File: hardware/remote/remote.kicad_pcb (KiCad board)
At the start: 2 copper layers, 106.7 x 86.4 mm, 30 parts

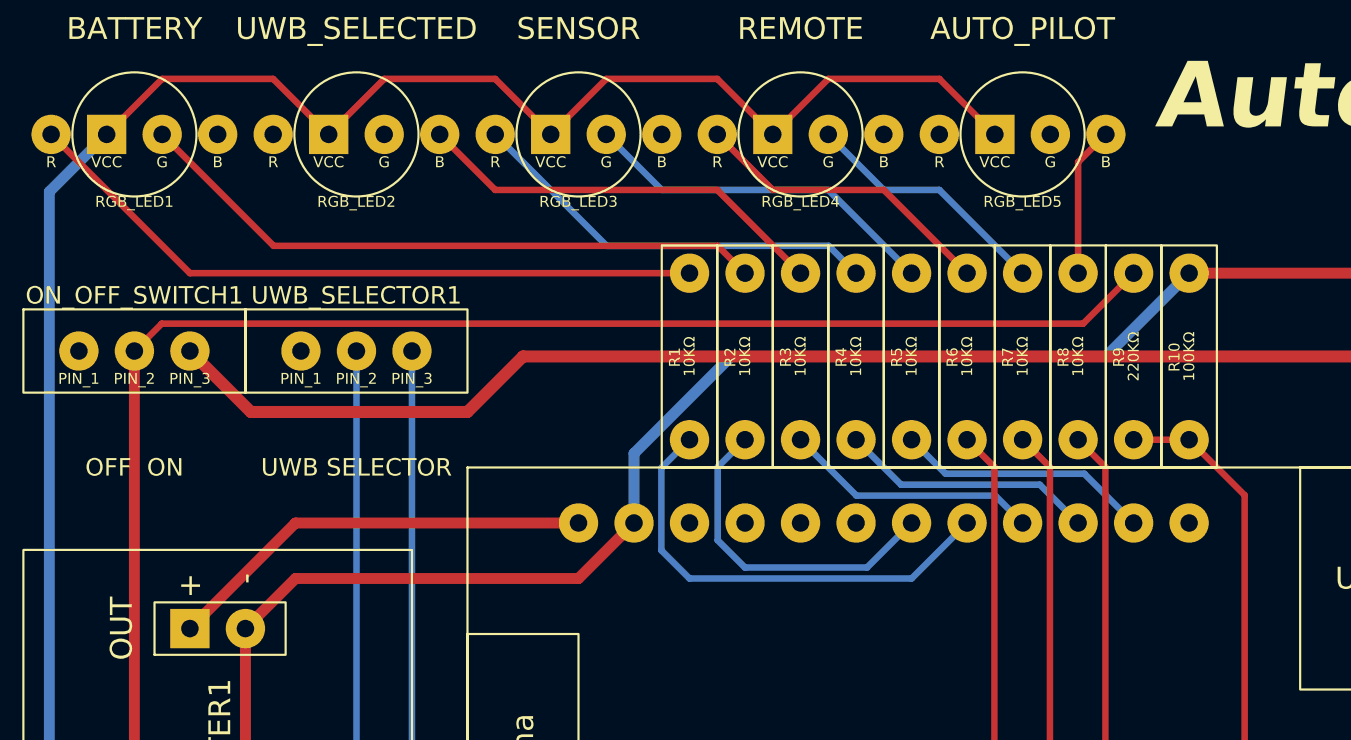
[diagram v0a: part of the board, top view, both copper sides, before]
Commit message: hardware: Update pcd design for better wiring clearance.
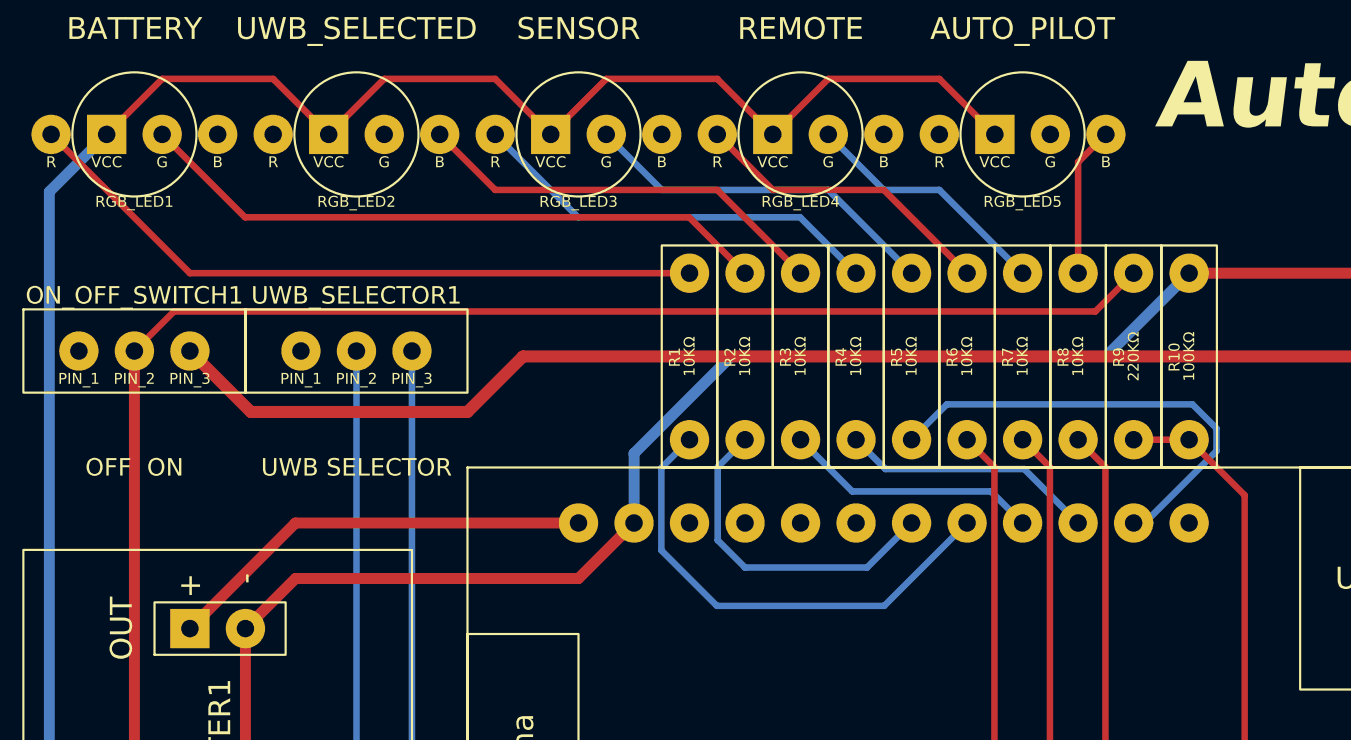
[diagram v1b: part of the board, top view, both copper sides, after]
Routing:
- net Net-(ESP32_UWB1-IO22): track 11.7 -> 22.0 mm
- net Net-(ESP32_UWB1-IO16): track 21.2 -> 22.2 mm
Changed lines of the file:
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@@
+	)
+	(segment
+		(start 70.657127 32.250873)
+		(end 72.409 30.499)
+		(width 0.3)
+		(layer "F.Cu")
+		(net 8)
 	)
 	(segment
 		(start 26.689 34.060058)
-		(end 27.94 32.809058)
+		(end 28.498185 32.250873)
 		(width 0.3)
 		(layer "F.Cu")
@@
 	)
 	(segment
-		(start 27.94 32.809058)
-		(end 70.098942 32.809058)
-		(width 0.3)
-		(layer "F.Cu")
-		(net 8)
-	)
-	(segment
-		(start 70.098942 32.809058)
-		(end 72.409 30.499)
+		(start 28.498185 32.250873)
+		(end 70.657127 32.250873)
 		(width 0.3)
 		(layer "F.Cu")
@@
 	)
 	(segment
-		(start 33.058 29.248)
-		(end 53.378 29.248)
+		(start 52.07 27.94)
+		(end 54.629 30.499)
 		(width 0.3)
 		(layer "F.Cu")
@@
 	)
 	(segment
+		(start 31.75 27.94)
+		(end 52.07 27.94)
+		(width 0.3)
+		(layer "F.Cu")
+		(net 37)
+	)
+	(segment
 		(start 27.959 24.149)
-		(end 33.058 29.248)
-		(width 0.3)
-		(layer "F.Cu")
-		(net 37)
-	)
-	(segment
-		(start 53.378 29.248)
-		(end 54.629 30.499)
+		(end 31.75 27.94)
 		(width 0.3)
 		(layer "F.Cu")
@@
 	)
 	(segment
-		(start 59.728 40.678)
-		(end 66.078 40.678)
+		(start 65.88331 40.48331)
+		(end 67.329 41.929)
 		(width 0.3)
 		(layer "B.Cu")
@@
 	)
 	(segment
+		(start 59.53331 40.48331)
+		(end 65.88331 40.48331)
+		(width 0.3)
+		(layer "B.Cu")
+		(net 44)
+	)
+	(segment
 		(start 57.169 38.119)
-		(end 59.728 40.678)
+		(end 59.53331 40.48331)
 		(width 0.3)
 		(layer "B.Cu")
@@
 	)
 	(segment
-		(start 66.078 40.678)
-		(end 67.329 41.929)
-		(width 0.3)
-		(layer "B.Cu")
-		(net 44)
+		(start 61.049231 39.459231)
+		(end 67.399231 39.459231)
+		(width 0.3)
+		(layer "B.Cu")
+		(net 45)
+	)
+	(segment
+		(start 67.399231 39.459231)
+		(end 69.869 41.929)
+		(width 0.3)
+		(layer "B.Cu")
+		(net 45)
 	)
 	(segment
 		(start 59.709 38.119)
-		(end 61.767 40.177)
+		(end 61.049231 39.459231)
 		(width 0.3)
 		(layer "B.Cu")
@@
 	)
 	(segment
-		(start 68.117 40.177)
-		(end 69.869 41.929)
-		(width 0.3)
-		(layer "B.Cu")
-		(net 45)
-	)
-	(segment
-		(start 61.767 40.177)
-		(end 68.117 40.177)
-		(width 0.3)
-		(layer "B.Cu")
-		(net 45)
-	)
-	(segment
 		(start 62.249 38.119)
-		(end 63.806 39.676)
+		(end 63.868 36.5)
 		(width 0.3)
 		(layer "B.Cu")
@@
 	)
 	(segment
-		(start 63.806 39.676)
-		(end 70.156 39.676)
+		(start 73.179818 41.929)
+		(end 72.409 41.929)
 		(width 0.3)
 		(layer "B.Cu")
@@
 	)
 	(segment
-		(start 70.156 39.676)
+		(start 75.099182 36.5)
+		(end 76.2 37.600818)
+		(width 0.3)
+		(layer "B.Cu")
+		(net 46)
+	)
+	(segment
+		(start 72.908182 41.929)
 		(end 72.409 41.929)
 		(width 0.3)
@@
 	)
 	(segment
-		(start 48.298 29.248)
-		(end 58.458 29.248)
+		(start 76.2 38.637182)
+		(end 72.908182 41.929)
+		(width 0.3)
+		(layer "B.Cu")
+		(net 46)
+	)
+	(segment
+		(start 63.868 36.5)
+		(end 75.099182 36.5)
+		(width 0.3)
+		(layer "B.Cu")
+		(net 46)
+	)
+	(segment
+		(start 76.2 37.600818)
+		(end 76.2 38.637182)
+		(width 0.3)
+		(layer "B.Cu")
+		(net 46)
+	)
+	(segment
+		(start 46.99 27.94)
+		(end 57.15 27.94)
 		(width 0.3)
 		(layer "B.Cu")
@@
 	(segment
 		(start 43.199 24.149)
-		(end 48.298 29.248)
+		(end 46.99 27.94)
 		(width 0.3)
 		(layer "B.Cu")
@@
 	)
 	(segment
-		(start 58.458 29.248)
+		(start 57.15 27.94)
 		(end 59.709 30.499)
 		(width 0.3)
@@
 	)
 	(segment
-		(start 52.089 44.469)
-		(end 62.249 44.469)
+		(start 50.8 43.18)
+		(end 53.34 45.72)
+		(width 0.3)
+		(layer "B.Cu")
+		(net 75)
+	)
+	(segment
+		(start 53.34 45.72)
+		(end 60.998 45.72)
+		(width 0.3)
+		(layer "B.Cu")
+		(net 75)
+	)
+	(segment
+		(start 60.998 45.72)
+		(end 64.789 41.929)
 		(width 0.3)
 		(layer "B.Cu")
@@
 		(width 0.3)
 		(layer "B.Cu")
-		(net 75)
-	)
-	(segment
-		(start 50.8 43.18)
-		(end 52.089 44.469)
-		(width 0.3)
-		(layer "B.Cu")
-		(net 75)
-	)
-	(segment
-		(start 62.249 44.469)
-		(end 64.789 41.929)
-		(width 0.3)
-		(layer "B.Cu")

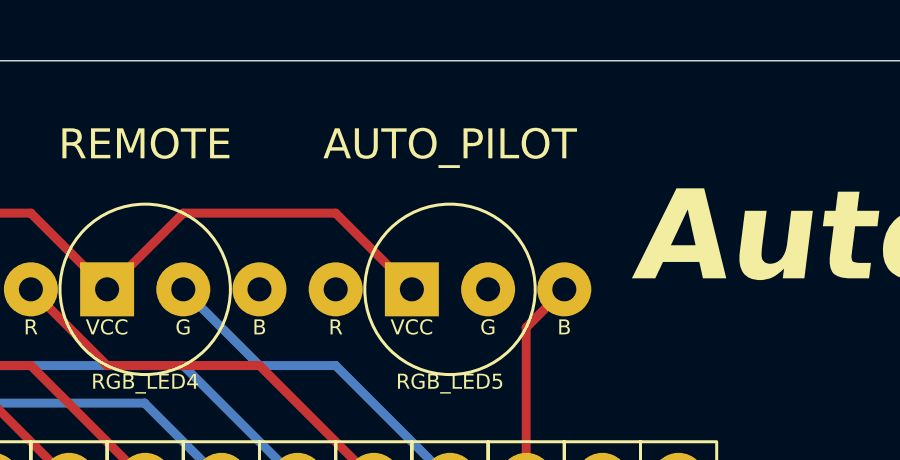
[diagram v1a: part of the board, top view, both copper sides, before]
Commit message: hardware: Revise the drive mode naming.
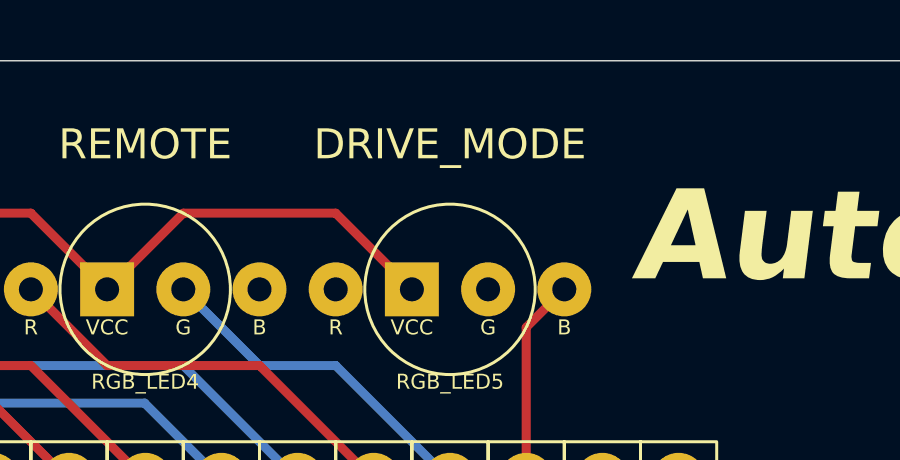
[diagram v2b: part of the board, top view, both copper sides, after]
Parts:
- RGB_LED5: value AUTO_PILOT -> DRIVE_MODE
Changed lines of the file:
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@@
 			)
 		)
-		(property "Value" "AUTO_PILOT"
+		(property "Value" "DRIVE_MODE"
 			(at 0 -4.831058 0)
 			(unlocked yes)

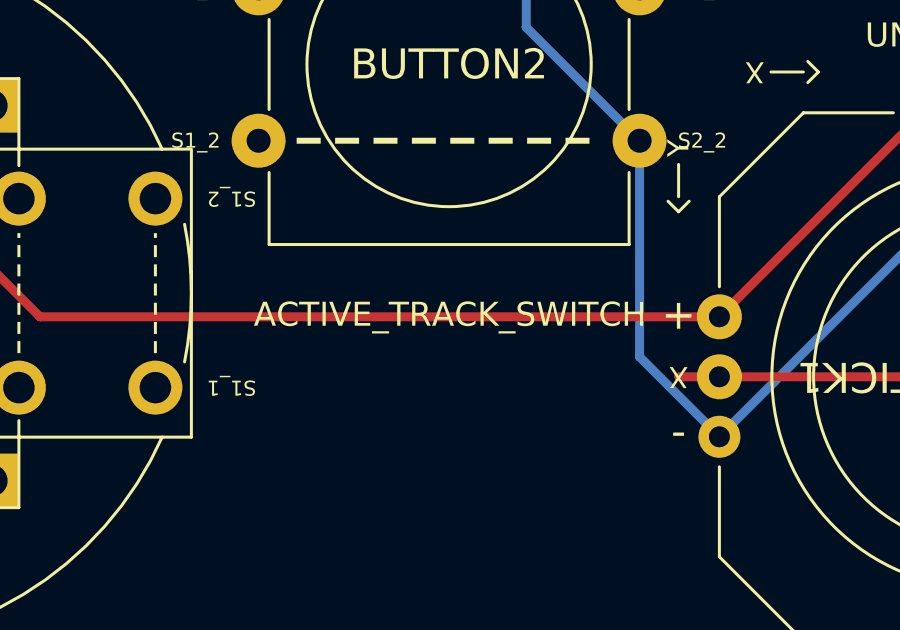
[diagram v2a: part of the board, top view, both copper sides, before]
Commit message: hardware: Update remote gimbal fn button naming.
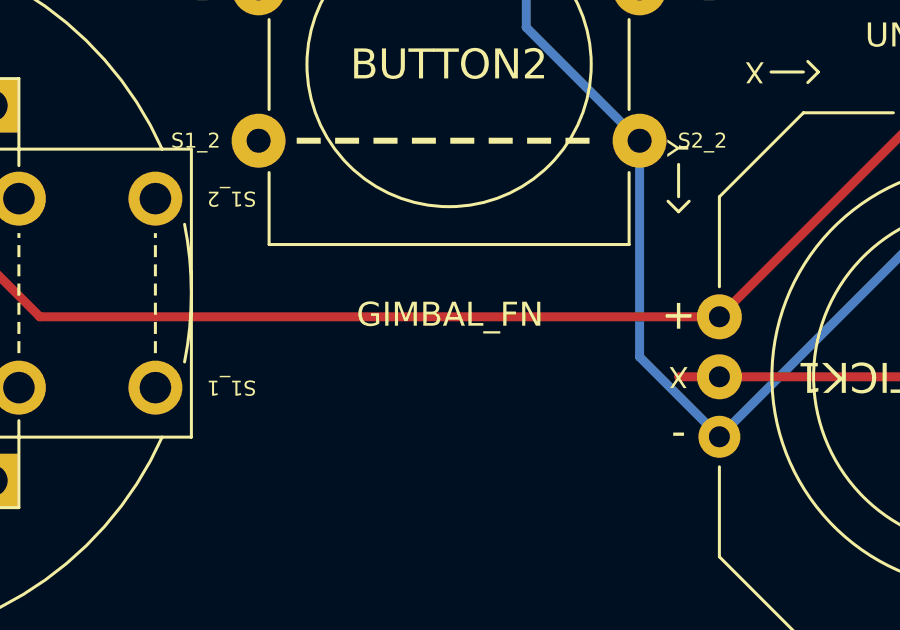
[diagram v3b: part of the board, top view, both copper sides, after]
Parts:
- BUTTON2: value ACTIVE_TRACK_SWITCH -> GIMBAL_FN
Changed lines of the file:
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@@
 			)
 		)
-		(property "Value" "ACTIVE_TRACK_SWITCH"
+		(property "Value" "GIMBAL_FN"
 			(at 0.03 7.868942 0)
 			(unlocked yes)
